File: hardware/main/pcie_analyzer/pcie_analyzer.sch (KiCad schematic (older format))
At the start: 50 parts, among them J1 HDR40, J2 HDR40, J3 Conn_Coaxial, J4 Conn_Coaxial, J5 Conn_Coaxial, J6 Conn_Coaxial, J7 Conn_Coaxial, J8 Conn_Coaxial

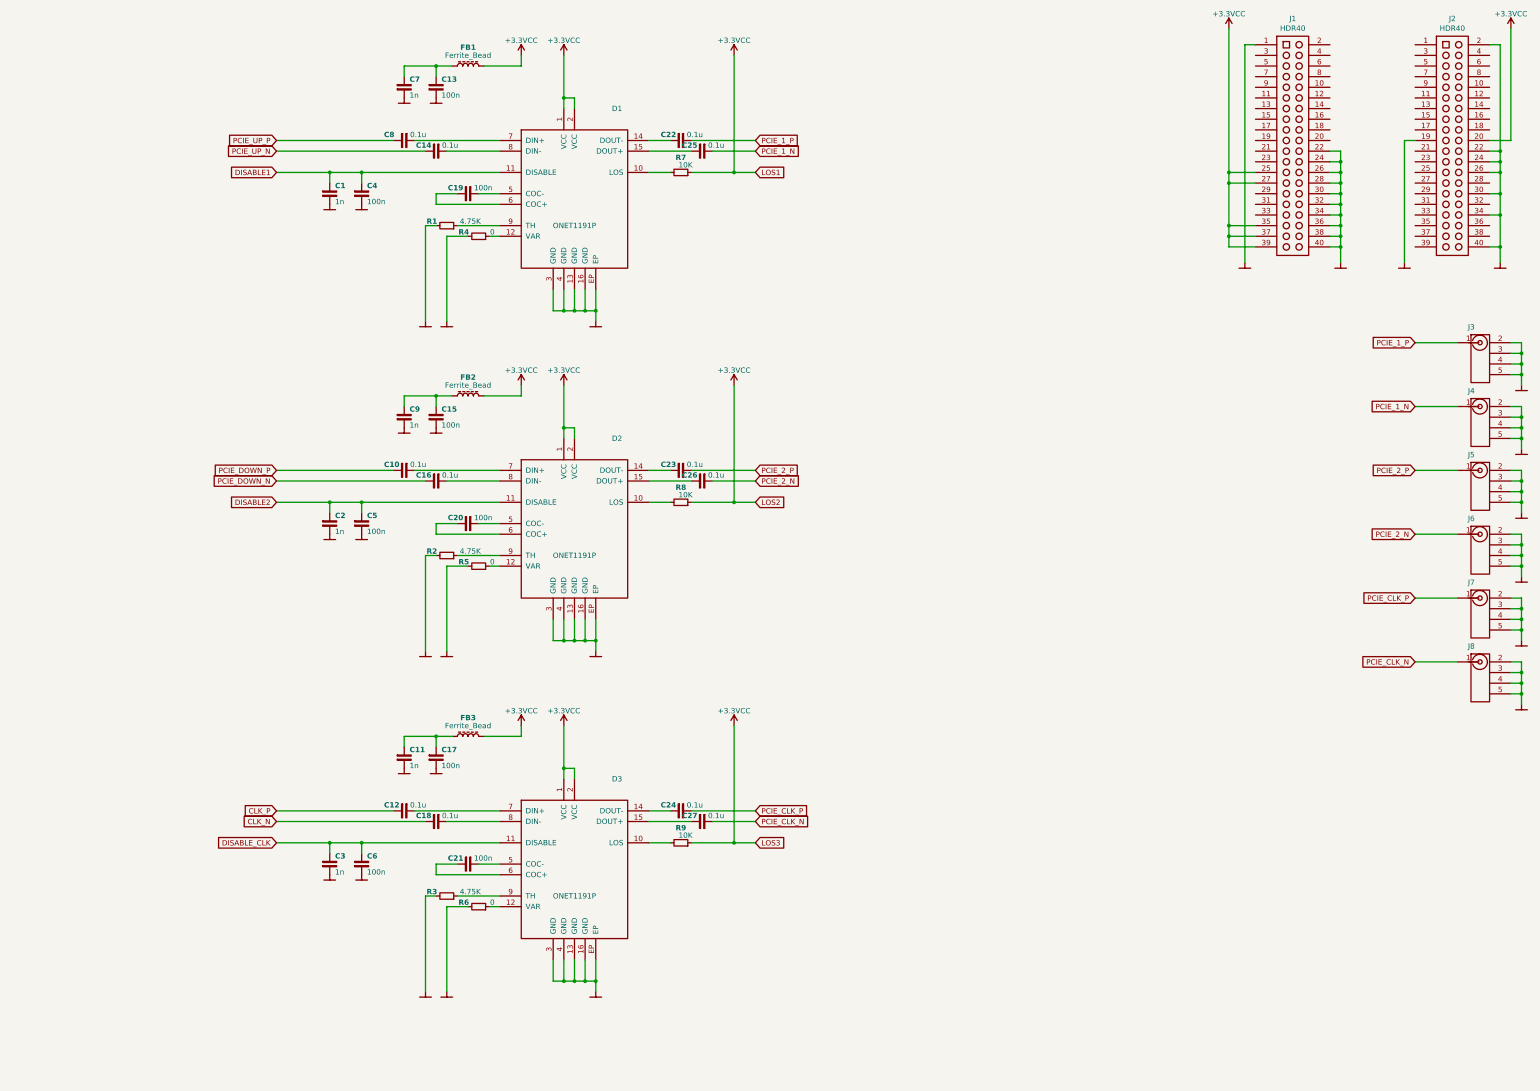
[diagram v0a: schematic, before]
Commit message: shema error correction
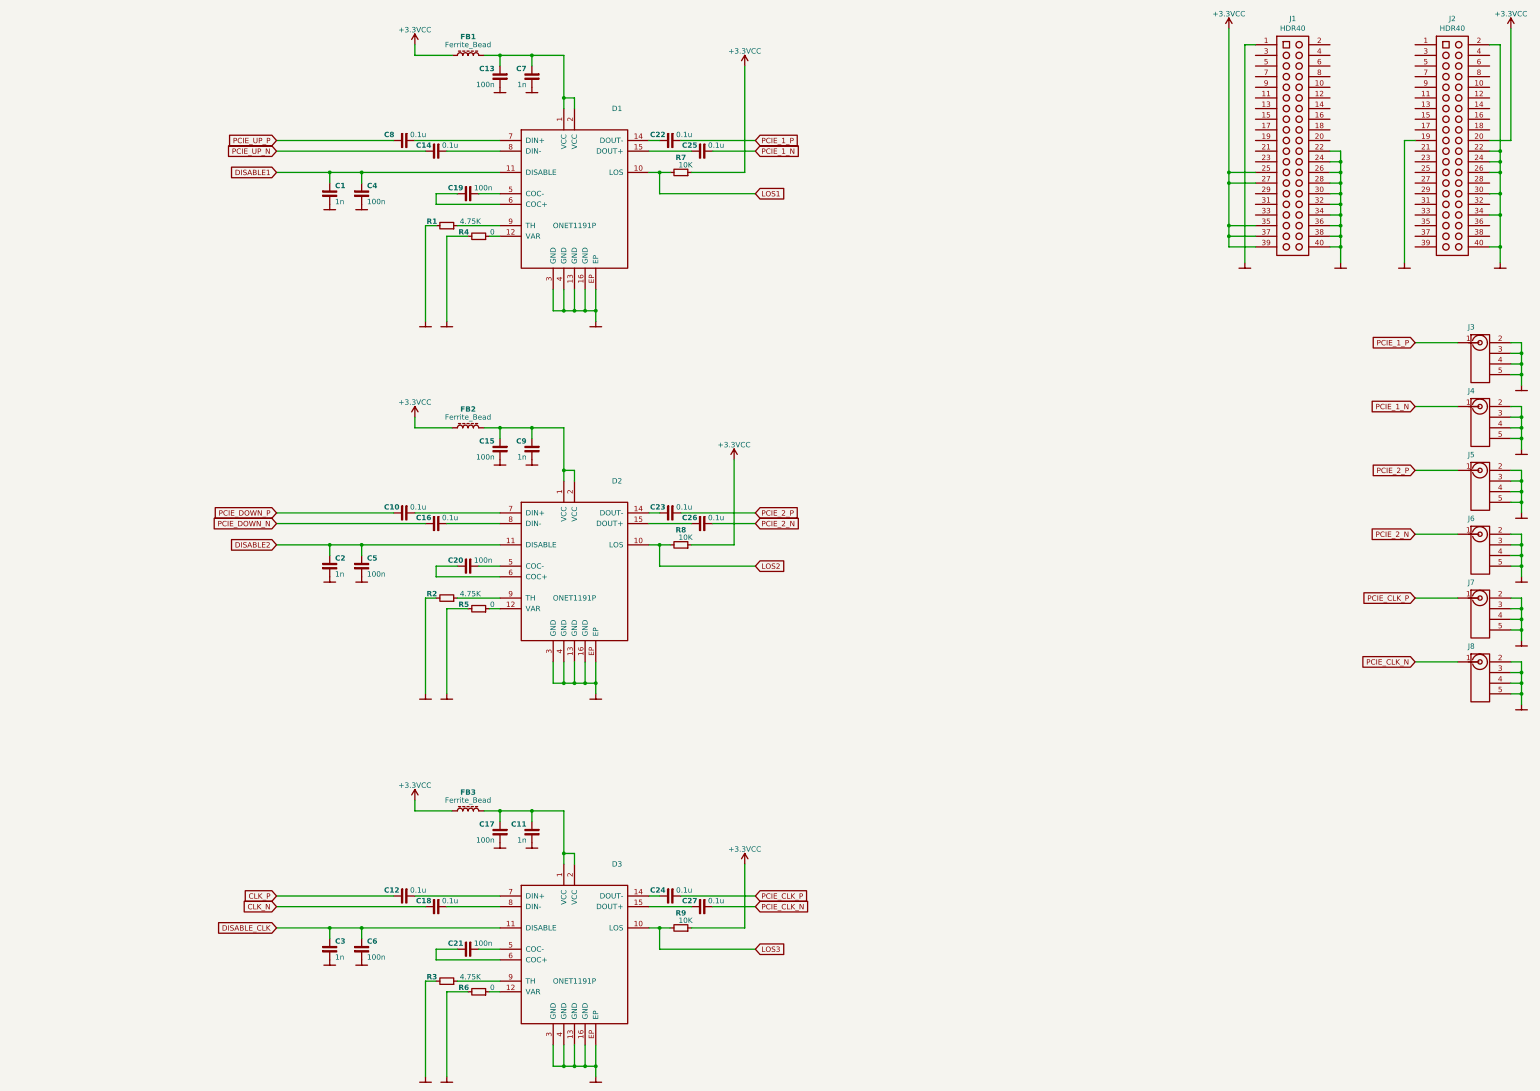
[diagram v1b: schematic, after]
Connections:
- net +3.3VCC: no longer D1.1 (VCC), D1.2 (VCC), D2.1 (VCC), D2.2 (VCC), D3.1 (VCC), D3.2 (VCC)
- net LOS1: now reaches D1.10 (LOS), R7.1
- net at C13.1, C7.1, FB1.1: now also D1.1 (VCC), D1.2 (VCC)
- net LOS2: now reaches D2.10 (LOS), R8.1
- net at C15.1, C9.1, FB2.1: now also D2.1 (VCC), D2.2 (VCC)
- net LOS3: now reaches D3.10 (LOS), R9.1
- net at C11.1, C17.1, FB3.1: now also D3.1 (VCC), D3.2 (VCC)
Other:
- moved on the sheet: C10, C11, C12, C13, C15, C16, C17, C18, C2, C20, C21, C22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

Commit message: pcb work
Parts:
- added ST1: AXIAL_CABLE_SL8800_08, ecp5_pcie_analyzer:AXIAL_CABLE_SL8800_08, symbol pcie_analyzer:AXIAL_CABLE_SL8800_08
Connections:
- net CLK_N: now also ST1.6
- net CLK_P: now also ST1.5
- net GND: now also ST1.M
- net PCIE_DOWN_N: now also ST1.4
- net PCIE_DOWN_P: now also ST1.3
- net PCIE_UP_N: now also ST1.2
- net PCIE_UP_P: now also ST1.1
- no-connect marks 0 -> 2
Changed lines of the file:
@@
 Wire Wire Line
 	7800 5100 7800 5900
+$Comp
+L pcie_analyzer:AXIAL_CABLE_SL8800_08 ST1
+U 1 1 611C5899
+P 1800 2000
+F 0 "ST1" H 2100 2150 50  0000 C CNN
+F 1 "AXIAL_CABLE_SL8800_08" H 2100 400 50  0000 C CNN
+F 2 "ecp5_pcie_analyzer:AXIAL_CABLE_SL8800_08" H 2200 400 50  0001 C CNN
+F 3 "" H 2000 1800 50  0001 C CNN
+	1    1800 2000
+	-1   0    0    -1
+$EndComp
+$Comp
+L pcie_analyzer:GND #PWR0126
+U 1 1 611DB058
+P 2000 3800
+F 0 "#PWR0126" H 1995 3630 50  0001 C CNN
+F 1 "GND" H 2000 3700 50  0001 C CNN
+F 2 "" H 2000 3800 50  0001 C CNN
+F 3 "" H 2000 3800 50  0001 C CNN
+	1    2000 3800
+	1    0    0    -1
+$EndComp
+Wire Wire Line
+	1800 3400 2000 3400
+Wire Wire Line
+	2000 3400 2000 3800
+Wire Wire Line
+	1800 2000 2000 2000
+Wire Wire Line
+	2000 2000 2000 3400
+Connection ~ 2000 3400
+Text GLabel 2200 2200 2    50   Input ~ 0
+PCIE_UP_P
+Text GLabel 2200 2300 2    50   Input ~ 0
+PCIE_UP_N
+Text GLabel 2100 2500 2    50   Input ~ 0
+PCIE_DOWN_P
+Text GLabel 2100 2600 2    50   Input ~ 0
+PCIE_DOWN_N
+Text GLabel 2400 2800 2    50   Input ~ 0
+CLK_P
+Text GLabel 2400 2900 2    50   Input ~ 0
+CLK_N
+Wire Wire Line
+	1800 2200 2200 2200
+Wire Wire Line
+	1800 2300 2200 2300
+Wire Wire Line
+	1800 2500 2100 2500
+Wire Wire Line
+	1800 2600 2100 2600
+Wire Wire Line
+	1800 2800 2400 2800
+Wire Wire Line
+	1800 2900 2400 2900
+NoConn ~ 1800 3100
+NoConn ~ 1800 3200
 $EndSCHEMATC

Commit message: daily work
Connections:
- net DISABLE1: now also J1.11
- net DISABLE2: now also J1.13
- net DISABLE_CLK: now also J1.15
- net LOS1: now also J1.5
- net LOS2: now also J1.7
- net LOS3: now also J1.9
- net PCIE_DOWN_N: now also ST1.2; no longer ST1.4
- net PCIE_DOWN_P: now also ST1.1; no longer ST1.3
- net PCIE_UP_N: now also ST1.4; no longer ST1.2
- net PCIE_UP_P: now also ST1.3; no longer ST1.1
- no-connect marks 2 -> 51
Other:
- moved on the sheet: C1, C10, C11, C12, C13, C14, C15, C16, C17, C18, C19, C2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

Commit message: pcb work
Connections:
- net DISABLE1: now also J1.13; no longer J1.11
- net DISABLE2: now also J1.9; no longer J1.13
- net DISABLE_CLK: now also J1.5; no longer J1.15
- net LOS1: now also J1.15; no longer J1.5
- net LOS2: now also J1.11; no longer J1.7
- net LOS3: now also J1.7; no longer J1.9
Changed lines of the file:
@@
 Wire Wire Line
 	2300 2500 2700 2500
-Text GLabel 11800 2000 0    50   Input ~ 0
+Text GLabel 11800 2500 0    50   Input ~ 0
 LOS1
-Text GLabel 11800 2100 0    50   Input ~ 0
+Text GLabel 11800 2300 0    50   Input ~ 0
 LOS2
+Text GLabel 11800 2400 0    50   Input ~ 0
+DISABLE1
 Text GLabel 11800 2200 0    50   Input ~ 0
-LOS3
-Text GLabel 11800 2300 0    50   Input ~ 0
-DISABLE1
-Text GLabel 11800 2400 0    50   Input ~ 0
 DISABLE2
-Text GLabel 11800 2500 0    50   Input ~ 0
-DISABLE_CLK
 Wire Wire Line
 	11800 2000 12200 2000
@@
 NoConn ~ 14400 1900
 NoConn ~ 14400 2000
+Text GLabel 11800 2000 0    50   Input ~ 0
+DISABLE_CLK
+Text GLabel 11800 2100 0    50   Input ~ 0
+LOS3
 $EndSCHEMATC

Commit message: first release sch/pcb
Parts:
- added R10, R11: 0, ecp5_pcie_analyzer:R_0402, symbol pcie_analyzer:R
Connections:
- net GND: now also R10.2, R11.2; no longer ST1.M
- new net: R10.1, ST1.M
- new net: R11.1, ST1.M
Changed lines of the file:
@@
 	2300 3300 2500 3300
 Wire Wire Line
-	2500 3300 2500 3700
-Wire Wire Line
-	2300 1900 2500 1900
-Wire Wire Line
-	2500 1900 2500 3300
-Connection ~ 2500 3300
-Text GLabel 2700 2400 2    50   Input ~ 0
+	2500 3300 2500 3400
+Text GLabel 2900 2400 2    50   Input ~ 0
 PCIE_UP_P
-Text GLabel 2900 2700 2    50   Input ~ 0
+Text GLabel 3100 2700 2    50   Input ~ 0
 CLK_P
-Text GLabel 2900 2800 2    50   Input ~ 0
+Text GLabel 3100 2800 2    50   Input ~ 0
 CLK_N
-Wire Wire Line
-	2300 2100 2700 2100
-Wire Wire Line
-	2300 2200 2700 2200
-Wire Wire Line
-	2300 2400 2700 2400
-Wire Wire Line
-	2300 2700 2900 2700
-Wire Wire Line
-	2300 2800 2900 2800
 NoConn ~ 2300 3000
 NoConn ~ 2300 3100
@@
 Wire Wire Line
 	5100 5600 6200 5600
-Text GLabel 2700 2200 2    50   Input ~ 0
+Text GLabel 2900 2200 2    50   Input ~ 0
 PCIE_DOWN_N
-Text GLabel 2700 2100 2    50   Input ~ 0
+Text GLabel 2900 2100 2    50   Input ~ 0
 PCIE_DOWN_P
 Wire Wire Line
@@
 	0    1    1    0
 $EndComp
-Text GLabel 2700 2500 2    50   Input ~ 0
+Text GLabel 2900 2500 2    50   Input ~ 0
 PCIE_UP_N
-Wire Wire Line
-	2300 2500 2700 2500
 Text GLabel 11800 2500 0    50   Input ~ 0
 LOS1
@@
 Text GLabel 11800 2100 0    50   Input ~ 0
 LOS3
+Wire Wire Line
+	2500 3600 2500 3700
+$Comp
+L pcie_analyzer:R R11
+U 1 1 6125E84F
+P 2700 3500
+F 0 "R11" H 2530 3620 50  0000 L CNB
+F 1 "0" H 2730 3370 50  0000 L CNN
+F 2 "ecp5_pcie_analyzer:R_0402" V 2630 3500 50  0001 C CNN
+F 3 "" H 2700 3500 50  0001 C CNN
+	1    2700 3500
+	1    0    0    -1
+$EndComp
+$Comp
+L pcie_analyzer:GND #PWR0127
+U 1 1 61278318
+P 2700 3700
+F 0 "#PWR0127" H 2695 3530 50  0001 C CNN
+F 1 "GND" H 2700 3600 50  0001 C CNN
+F 2 "" H 2700 3700 50  0001 C CNN
+F 3 "" H 2700 3700 50  0001 C CNN
+	1    2700 3700
+	1    0    0    -1
+$EndComp
+Wire Wire Line
+	2700 3600 2700 3700
+$Comp
+L pcie_analyzer:R R10
+U 1 1 6125D88C
+P 2500 3500
+F 0 "R10" H 2330 3620 50  0000 L CNB
+F 1 "0" H 2520 3370 50  0000 L CNN
+F 2 "ecp5_pcie_analyzer:R_0402" V 2430 3500 50  0001 C CNN
+F 3 "" H 2500 3500 50  0001 C CNN
+	1    2500 3500
+	1    0    0    -1
+$EndComp
+Wire Wire Line
+	2300 2100 2900 2100
+Wire Wire Line
+	2300 2200 2900 2200
+Wire Wire Line
+	2300 2400 2900 2400
+Wire Wire Line
+	2300 2500 2900 2500
+Wire Wire Line
+	2300 2700 3100 2700
+Wire Wire Line
+	2300 2800 3100 2800
+Wire Wire Line
+	2700 1900 2700 3400
+Wire Wire Line
+	2300 1900 2700 1900
 $EndSCHEMATC

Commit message: major design update
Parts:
- ST1: symbol pcie_analyzer:AXIAL_CABLE_SL8800_08 -> pcie_analyzer-rescue:AXIAL_CABLE_SL8800_08-pcie_analyzer
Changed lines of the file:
@@
 	13600 8600 13600 8700
 $Comp
-L pcie_analyzer:AXIAL_CABLE_SL8800_08 ST1
+L pcie_analyzer-rescue:AXIAL_CABLE_SL8800_08-pcie_analyzer ST1
 U 1 1 611C5899
 P 2300 1900
